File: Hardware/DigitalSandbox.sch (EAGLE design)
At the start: 80 parts, among them J1 AVR_SPI_PRG_6NS, Q1 MOSFET-N, Q2 MOSFET-P, U1 MCP73831, U2 ATMEGA328, U3 10K_LINEAR_SLIDE_POT_SMALL, U4 MCP9700, U5 FT232RLSSOP, U6 LIGHTSENSORALS, U7 V_REG_MIC52053.3V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

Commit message: fixed reset button orientation to work with standard push button
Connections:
- net GND: now also S1.3, S1.4; no longer S1.2
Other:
- note added: "v11"
- note removed: "v10"
- moved on the sheet: S1
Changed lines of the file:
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@@
 <wire x1="345.44" y1="86.36" x2="345.44" y2="139.7" width="0.4064" layer="97" style="shortdash"/>
 <wire x1="345.44" y1="86.36" x2="317.5" y2="86.36" width="0.4064" layer="97" style="shortdash"/>
-<text x="421.64" y="7.62" size="2.54" layer="94" font="vector">v10</text>
+<text x="421.64" y="7.62" size="2.54" layer="94" font="vector">v11</text>
 </plain>
 <instances>
@@
 <attribute name="VALUE" x="32.004" y="199.136" size="1.778" layer="96"/>
 </instance>
-<instance part="GND6" gate="1" x="35.56" y="162.56"/>
+<instance part="GND6" gate="1" x="35.56" y="160.02"/>
 <instance part="P+3" gate="1" x="45.72" y="187.96" smashed="yes">
 <attribute name="VALUE" x="44.704" y="191.516" size="1.778" layer="96"/>
@@
 </instance>
 <instance part="GND12" gate="1" x="81.28" y="251.46"/>
-<instance part="S1" gate="S" x="30.48" y="170.18" rot="MR0"/>
+<instance part="S1" gate="S" x="35.56" y="172.72" rot="MR270"/>
 <instance part="GND13" gate="1" x="68.58" y="226.06"/>
 <instance part="U4" gate="G$1" x="162.56" y="182.88"/>
@@
 </segment>
 <segment>
-<pinref part="GND6" gate="1" pin="GND"/>
-<pinref part="S1" gate="S" pin="2"/>
-<wire x1="35.56" y1="165.1" x2="35.56" y2="167.64" width="0.1524" layer="91"/>
-</segment>
-<segment>
 <wire x1="401.32" y1="175.26" x2="398.78" y2="175.26" width="0.1524" layer="91"/>
 <wire x1="398.78" y1="175.26" x2="398.78" y2="172.72" width="0.1524" layer="91"/>
@@
 <pinref part="JP1" gate="G$1" pin="2"/>
 <wire x1="81.28" y1="254" x2="81.28" y2="259.08" width="0.1524" layer="91"/>
+</segment>
+<segment>
+<pinref part="S1" gate="S" pin="3"/>
+<pinref part="GND6" gate="1" pin="GND"/>
+<wire x1="35.56" y1="167.64" x2="35.56" y2="165.1" width="0.1524" layer="91"/>
+<pinref part="S1" gate="S" pin="4"/>
+<wire x1="35.56" y1="165.1" x2="35.56" y2="162.56" width="0.1524" layer="91"/>
+<wire x1="38.1" y1="167.64" x2="38.1" y2="165.1" width="0.1524" layer="91"/>
+<wire x1="38.1" y1="165.1" x2="35.56" y2="165.1" width="0.1524" layer="91"/>
+<junction x="35.56" y="165.1"/>
 </segment>
 </net>
@@
 <net name="RST" class="0">
 <segment>
+<wire x1="33.02" y1="180.34" x2="35.56" y2="180.34" width="0.1524" layer="91"/>
 <wire x1="35.56" y1="180.34" x2="48.26" y2="180.34" width="0.1524" layer="91"/>
 <wire x1="27.94" y1="180.34" x2="33.02" y2="180.34" width="0.1524" layer="91"/>
-<junction x="35.56" y="180.34"/>
 <label x="38.1" y="180.34" size="1.778" layer="95"/>
 <pinref part="U2" gate="G$1" pin="PC6(/RESET)"/>
 <pinref part="R2" gate="G$1" pin="1"/>
 <pinref part="C1" gate="G$1" pin="2"/>
-<pinref part="S1" gate="S" pin="1"/>
-<wire x1="33.02" y1="180.34" x2="35.56" y2="180.34" width="0.1524" layer="91"/>
-<wire x1="35.56" y1="180.34" x2="35.56" y2="170.18" width="0.1524" layer="91"/>
 <wire x1="33.02" y1="182.88" x2="33.02" y2="180.34" width="0.1524" layer="91"/>
 <junction x="33.02" y="180.34"/>
-</segment>
-<segment>
+<pinref part="S1" gate="S" pin="1"/>
+<wire x1="35.56" y1="180.34" x2="35.56" y2="177.8" width="0.1524" layer="91"/>
+<junction x="35.56" y="180.34"/>
+</segment>
+<segment>

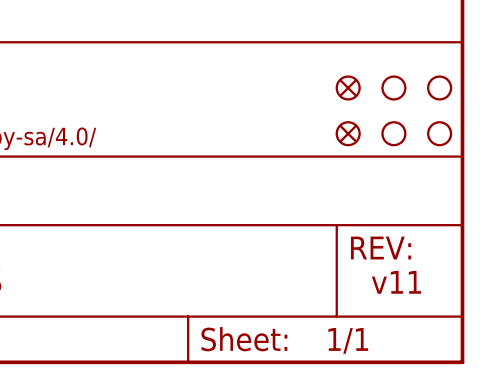
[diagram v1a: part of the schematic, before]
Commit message: Chg to v12, thicken logo/art borders
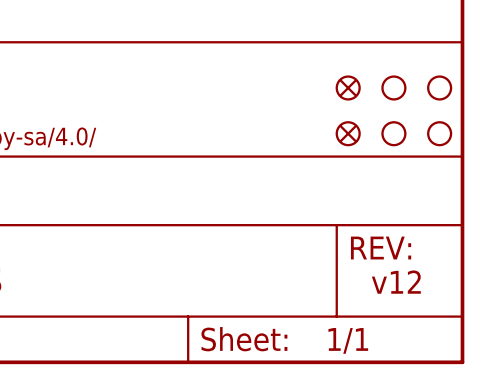
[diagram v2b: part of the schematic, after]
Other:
- note added: "v12"
- note removed: "v11"
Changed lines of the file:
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@@
 <?xml version="1.0" encoding="utf-8"?>
 <!DOCTYPE eagle SYSTEM "eagle.dtd">
-<eagle version="6.5.0">
+<eagle version="7.3.0">
 <drawing>
 <settings>
@@
 <layer number="56" name="wert" color="7" fill="1" visible="no" active="no"/>
 <layer number="57" name="tCAD" color="7" fill="1" visible="no" active="no"/>
+<layer number="59" name="tCarbon" color="7" fill="1" visible="no" active="no"/>
+<layer number="60" name="bCarbon" color="7" fill="1" visible="no" active="no"/>
+<layer number="90" name="Modules" color="5" fill="1" visible="yes" active="yes"/>
 <layer number="91" name="Nets" color="2" fill="1" visible="yes" active="yes"/>
 <layer number="92" name="Busses" color="1" fill="1" visible="yes" active="yes"/>
@@
 <layer number="127" name="_tValues" color="7" fill="1" visible="yes" active="yes"/>
 <layer number="128" name="_bValues" color="7" fill="1" visible="yes" active="yes"/>
+<layer number="129" name="Mask" color="7" fill="1" visible="yes" active="yes"/>
 <layer number="131" name="tAdjust" color="7" fill="1" visible="yes" active="yes"/>
 <layer number="132" name="bAdjust" color="7" fill="1" visible="yes" active="yes"/>
@@
 <layer number="223" name="223bmp" color="24" fill="1" visible="no" active="no"/>
 <layer number="224" name="224bmp" color="25" fill="1" visible="no" active="no"/>
+<layer number="225" name="225bmp" color="7" fill="1" visible="yes" active="yes"/>
+<layer number="226" name="226bmp" color="7" fill="1" visible="yes" active="yes"/>
+<layer number="227" name="227bmp" color="7" fill="1" visible="yes" active="yes"/>
+<layer number="228" name="228bmp" color="7" fill="1" visible="yes" active="yes"/>
+<layer number="229" name="229bmp" color="7" fill="1" visible="yes" active="yes"/>
+<layer number="230" name="230bmp" color="7" fill="1" visible="yes" active="yes"/>
+<layer number="231" name="231bmp" color="7" fill="1" visible="yes" active="yes"/>
 <layer number="248" name="Housing" color="7" fill="1" visible="yes" active="yes"/>
 <layer number="249" name="Edge" color="7" fill="1" visible="yes" active="yes"/>
@@
 <layer number="251" name="SMDround" color="12" fill="11" visible="no" active="no"/>
 <layer number="254" name="cooling" color="7" fill="1" visible="yes" active="yes"/>
+<layer number="255" name="routoute" color="7" fill="1" visible="yes" active="yes"/>
 </layers>
-<schematic>
+<schematic xreflabel="%F%N/%S" xrefpart="1_/%S.%C%R">
 <attributes>
 </attributes>
@@
 <wire x1="345.44" y1="86.36" x2="345.44" y2="139.7" width="0.4064" layer="97" style="shortdash"/>
 <wire x1="345.44" y1="86.36" x2="317.5" y2="86.36" width="0.4064" layer="97" style="shortdash"/>
-<text x="421.64" y="7.62" size="2.54" layer="94" font="vector">v11</text>
+<text x="421.64" y="7.62" size="2.54" layer="94" font="vector">v12</text>
 </plain>
 <instances>
